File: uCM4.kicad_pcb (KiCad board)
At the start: 2 copper layers, 55 x 40 mm, 30 parts, among them J1 Conn_01x03, J2 Ethernet, J3 Micro_SD_Card, J4 USB_B_Micro, SW1 SW_DIP_x01, SW2 SW_DIP_x01, U1 RT9742GGJ5, U2 74LVC1G07, U3 TPD4EUSB30

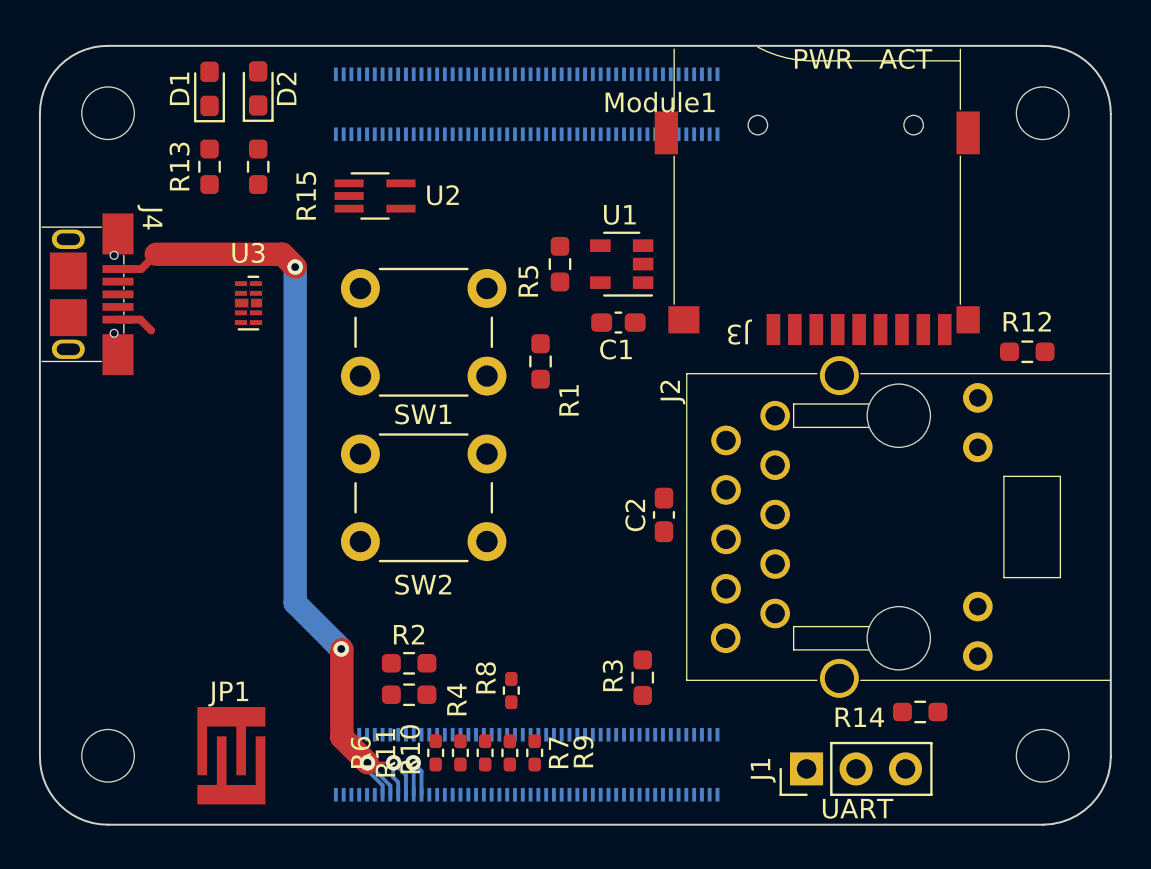
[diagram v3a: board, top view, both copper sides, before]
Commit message: Draw stands on Micro SD connector
It conflicts with mounting hole and this is the only problem on the
whole board at the moment. There are two ways to solve this, as it is
the only place where it (almost) fits:
1. Make ground plane of Micro SD a bit smaller - in the worst case will
   not mount connector to PCB
2. Remove mounting hole of module - will make two boards a little bit
   less stable together

As of now it is undecided what option to take.
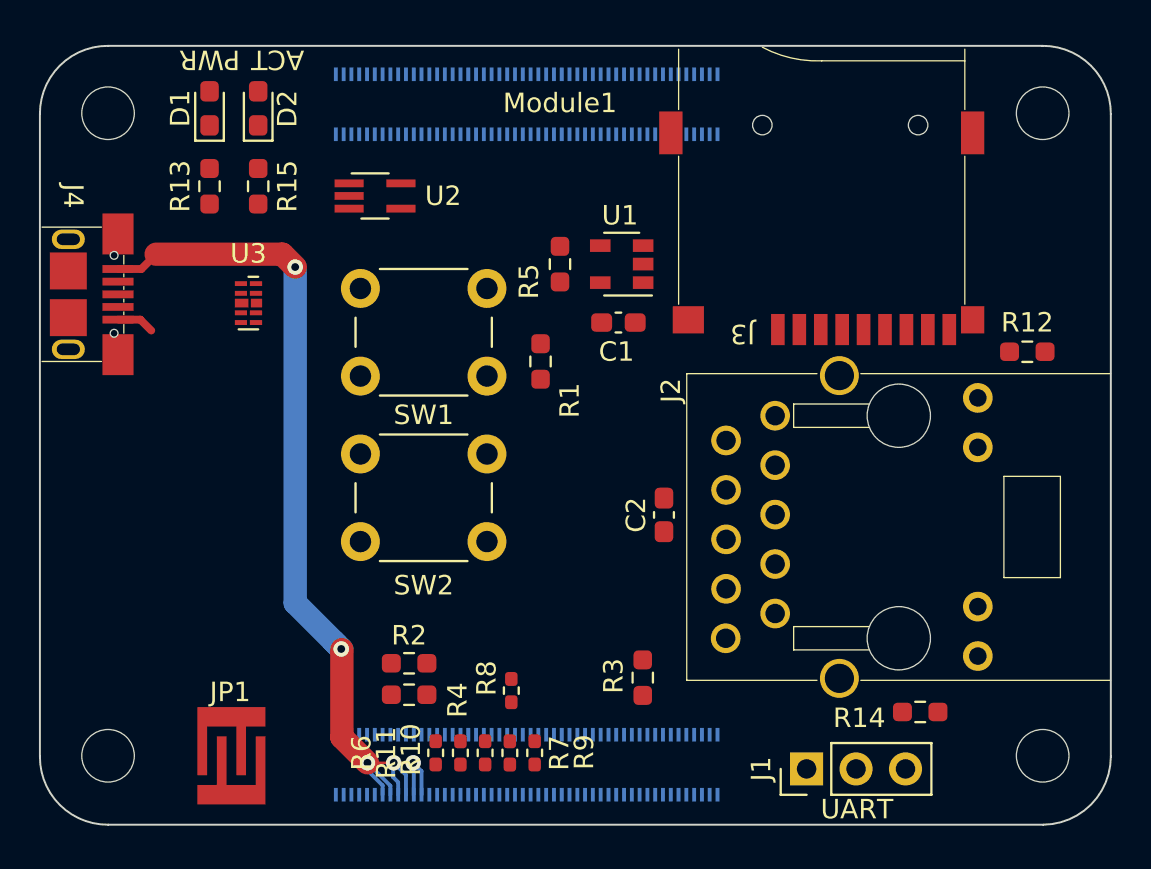
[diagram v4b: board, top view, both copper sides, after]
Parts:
- moved D2 1.02 mm to (149.0, 64.5)
- moved D1 1.00 mm to (146.5, 64.5)
- moved R13 1.00 mm to (146.5, 68.5)
- moved R15 1.00 mm to (149.0, 68.5)
- moved J3 0.23 mm to (177.9, 75.9)

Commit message: Route Micro SD connector
Hope this will not be moved anymore.
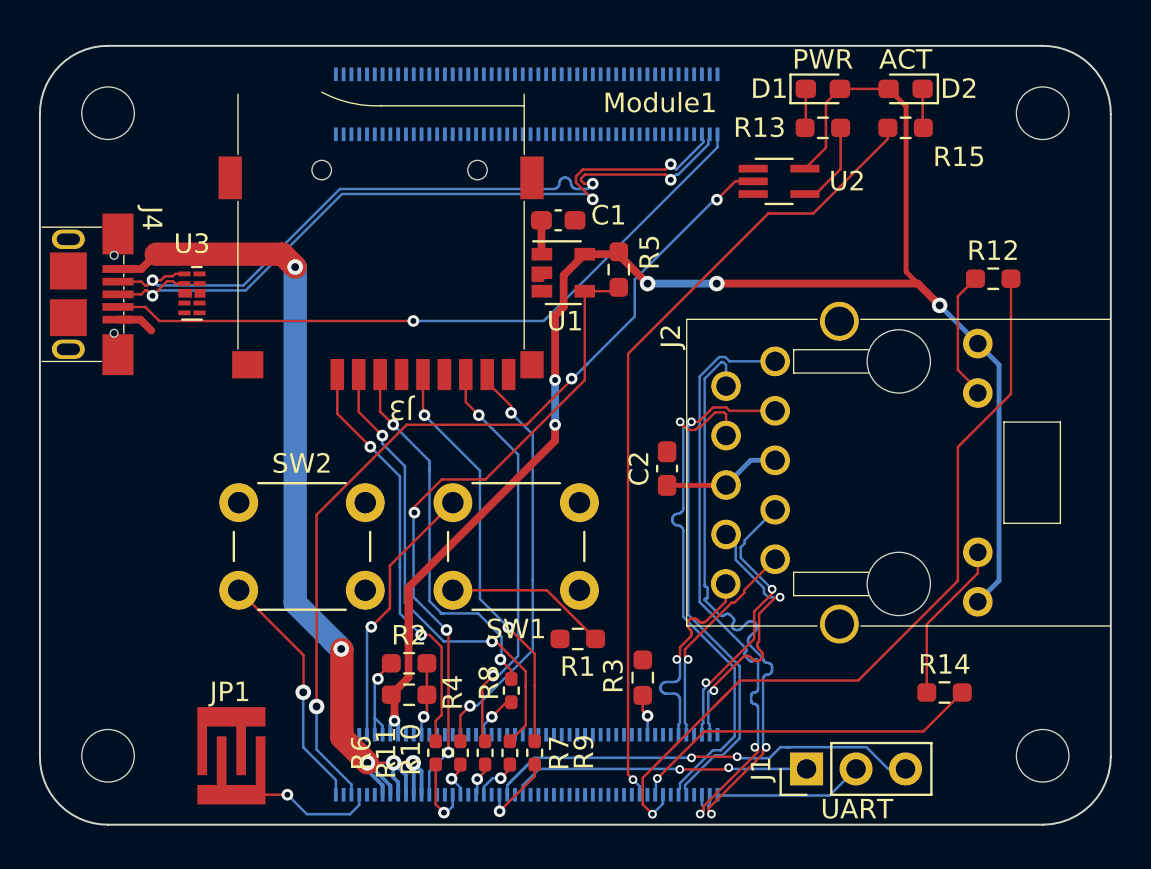
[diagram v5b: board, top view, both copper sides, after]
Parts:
- moved R15 33.4 mm to (182.2, 65.5), turned to 0 degrees
- moved D2 33.3 mm to (182.2, 63.5), turned to 180 degrees
- moved R13 31.6 mm to (178.0, 65.5), turned to 180 degrees
- moved D1 31.5 mm to (178.0, 63.5), turned to 0 degrees
- moved J3 22.7 mm to (155.3, 78.2)
- moved U2 20.8 mm to (175.8, 68.2)
- moved R1 14.4 mm to (165.4, 91.8), turned to 180 degrees
- moved SW1 12.0 mm to (165.5, 89.2)
- moved SW2 6.73 mm to (148.0, 84.8)
- moved C1 6.09 mm to (164.4, 70.2), turned to 180 degrees
- moved R12 4.14 mm to (186.8, 73.2), turned to 0 degrees
- moved R5 3.03 mm to (167.5, 72.8), turned to 90 degrees
- moved U1 3.03 mm to (164.7, 72.9), turned to 0 degrees
- moved U3 2.94 mm to (145.6, 74.0)
- moved J2 2.79 mm to (181.9, 83.2)
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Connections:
- net Net-(Module1-Pad57) renamed /SD_CLK
- net Net-(Module1-Pad61) renamed /SD_D3
- net Net-(Module1-Pad62) renamed /SD_CMD
- net Net-(Module1-Pad63) renamed /SD_D0
- net Net-(Module1-Pad67) renamed /SD_D1
- net Net-(Module1-Pad69) renamed /SD_D2
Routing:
- net +3V3: track 0.00 -> 87.6 mm, vias 0 -> 6
- net /nPWR_LED: track 0.00 -> 46.1 mm, vias 0 -> 3
- net Net-(Module1-Pad21): track 0.00 -> 41.5 mm, vias 0 -> 1
- net Net-(Module1-Pad15): track 0.00 -> 40.9 mm, vias 0 -> 1
- net /USB_P: track 0.00 -> 38.3 mm, vias 0 -> 3
- net /USB_N: track 0.00 -> 38.1 mm, vias 0 -> 3
- net Net-(J4-Pad4): track 0.00 -> 35.6 mm, vias 0 -> 1
- net /SD_EN: track 0.00 -> 34.0 mm, vias 0 -> 3
- net /Eth_P3_N: track 0.00 -> 31.3 mm, vias 0 -> 2
- net /Eth_P3_P: track 0.00 -> 31.3 mm, vias 0 -> 2
- net /Eth_P2_P: track 0.00 -> 26.4 mm, vias 0 -> 1
- net /Eth_P2_N: track 0.00 -> 26.4 mm, vias 0 -> 1
- net Net-(J3-Pad2): track 0.00 -> 24.4 mm, vias 0 -> 2
- net /TX: track 0.00 -> 24.1 mm, vias 0 -> 2
- net Net-(J3-Pad8): track 0.00 -> 21.6 mm, vias 0 -> 2
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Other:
- board text added: "1"
- board text added: "2"
- board text added: "3"
- board text added: "5"
- board text added: "7"
- board text added: "8"

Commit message: Reroute Ethernet and suroundings
All traces intersecting with Ethernet had to be removed to make
rerouting easier. Then Ethernet pairs were routed again. No length
adjustments has been done yet.
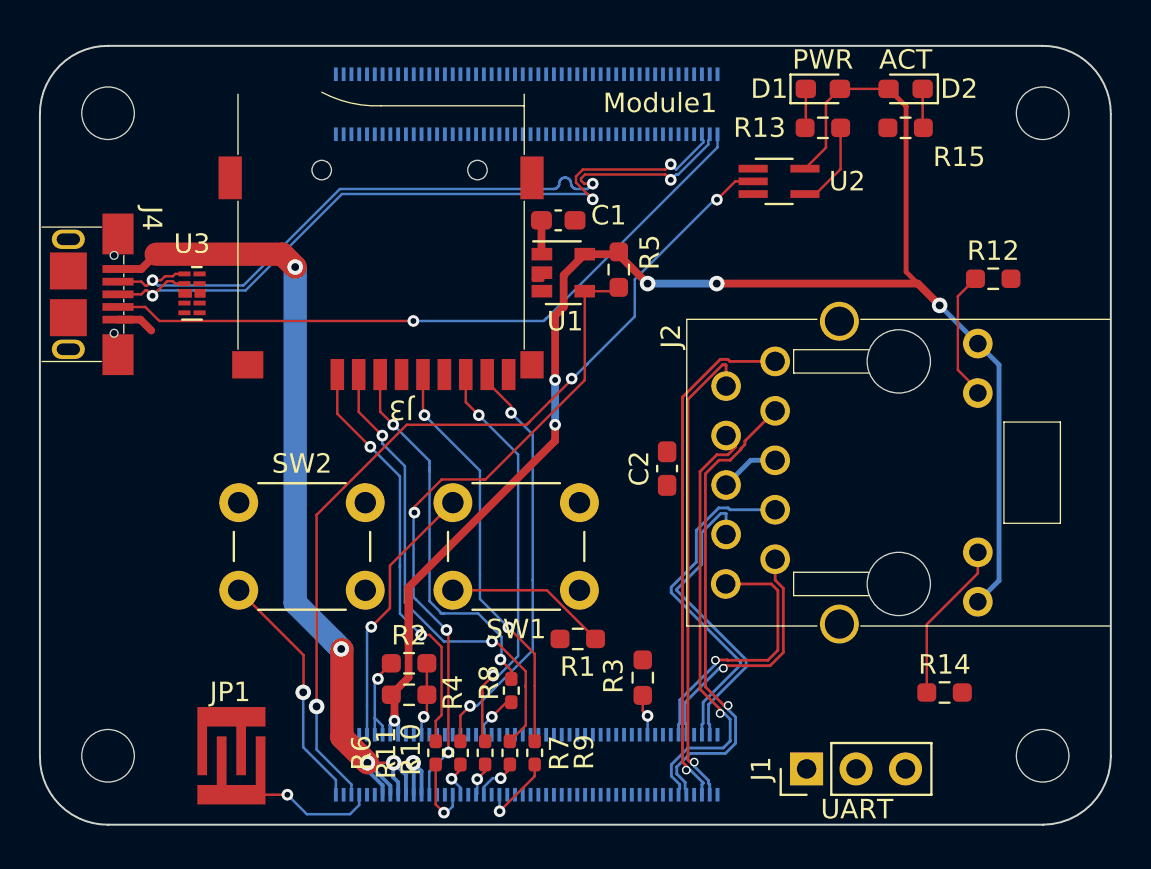
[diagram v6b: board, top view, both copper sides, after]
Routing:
- net Net-(Module1-Pad21): track 41.5 -> 0.00 mm, vias 1 -> 0
- net Net-(Module1-Pad15): track 40.9 -> 0.00 mm, vias 1 -> 0
- net /TX: track 24.1 -> 0.00 mm, vias 2 -> 0
- net Net-(Module1-Pad17): track 18.3 -> 0.00 mm, vias 1 -> 0
- net /RX: track 15.6 -> 0.00 mm, vias 2 -> 0
- net GND: track 10.1 -> 2.38 mm
- net /Eth_P3_P: track 31.3 -> 24.9 mm, vias 2 -> 1
- net /Eth_P3_N: track 31.3 -> 26.9 mm, vias 2 -> 1
- net /Eth_P2_P: track 26.4 -> 23.0 mm
- net /Eth_P1_N: track 14.6 -> 17.9 mm, vias 2 -> 0
- net Net-(C2-Pad1): track 6.08 -> 3.07 mm
- net /Eth_P0_P: track 11.2 -> 13.9 mm
- net /Eth_P2_N: track 26.4 -> 24.8 mm
- net /Eth_P0_N: track 11.2 -> 12.8 mm
- net /Eth_P1_P: track 14.6 -> 16.0 mm, vias 2 -> 0

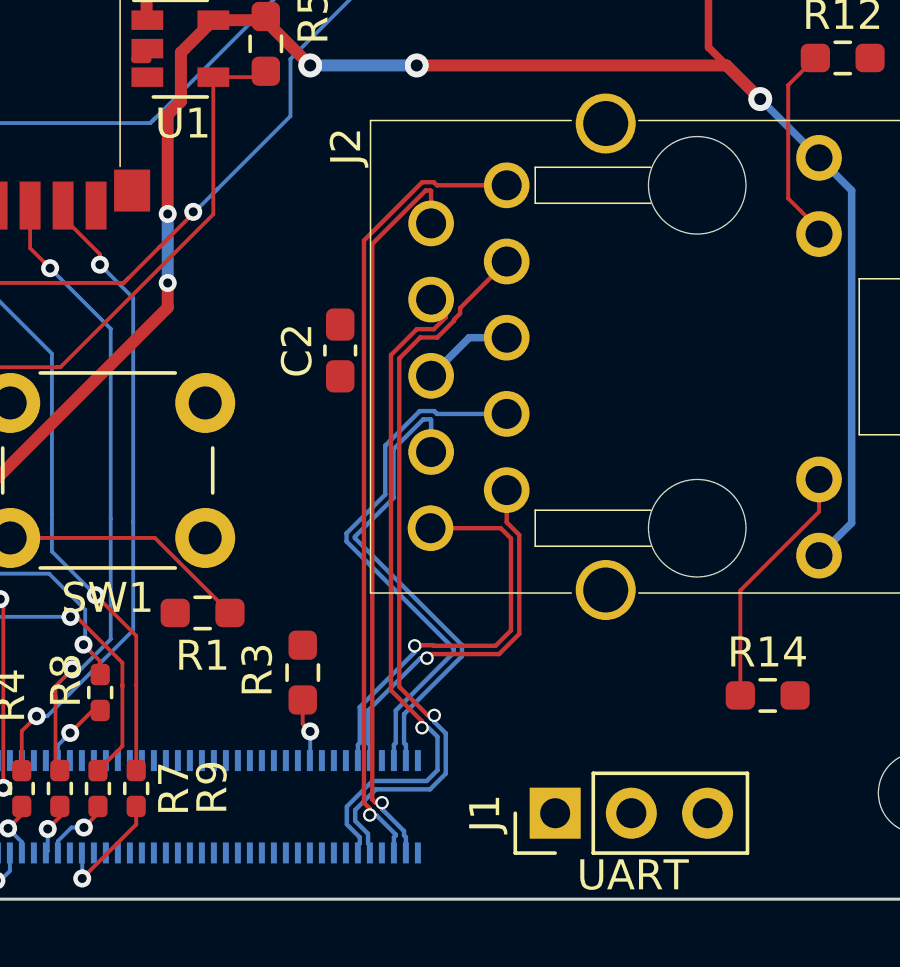
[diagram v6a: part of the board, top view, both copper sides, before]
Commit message: Adjust Ethernet pair and in-pair lengths
Almost complete - shortest path has in-pair difference of 0.8 mm. Let's
try again.
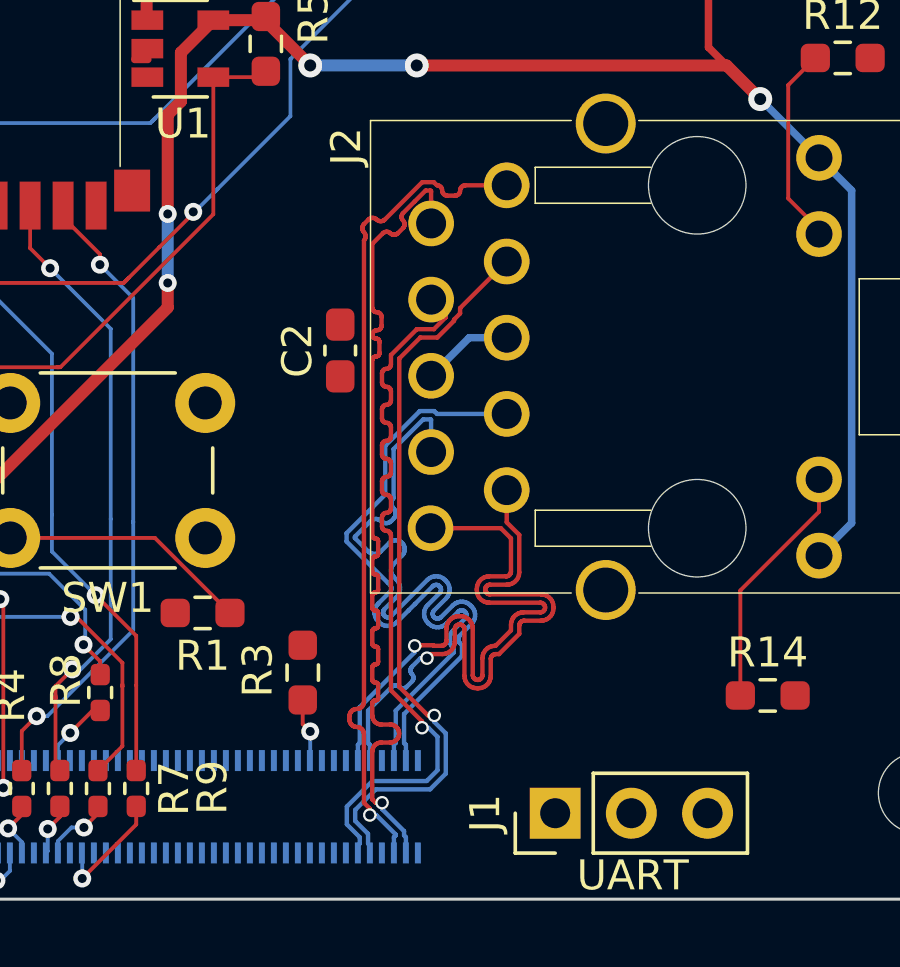
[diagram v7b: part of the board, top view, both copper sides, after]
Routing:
- net /Eth_P0_N: track 12.8 -> 20.5 mm
- net /Eth_P1_P: track 16.0 -> 23.6 mm
- net /Eth_P0_P: track 13.9 -> 21.3 mm
- net /Eth_P1_N: track 17.9 -> 23.5 mm
- net /Eth_P3_P: track 24.9 -> 28.3 mm
- net /Eth_P2_P: track 23.0 -> 24.7 mm
- net /Eth_P3_N: track 26.9 -> 28.2 mm

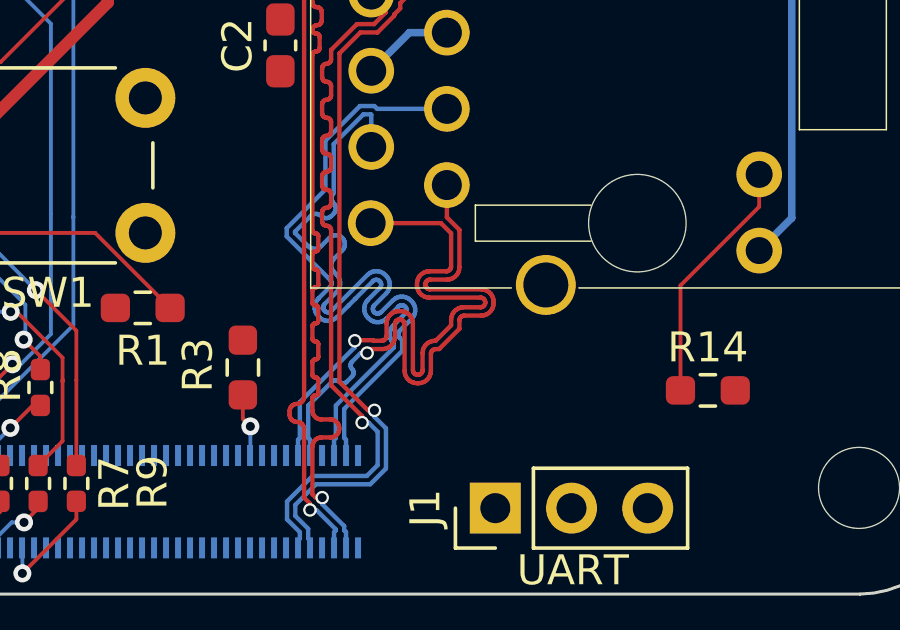
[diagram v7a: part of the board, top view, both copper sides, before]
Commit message: Fix zeroth Ethernet pair
Now it is in tolerance. Now it is a question, if another attempt for
pair-to-pair difference reduction makes any sense.
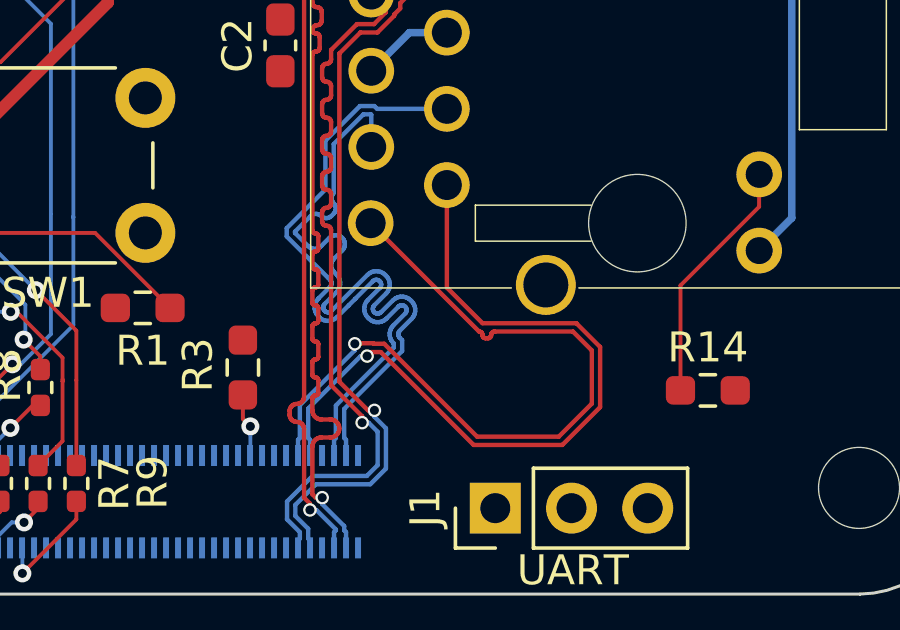
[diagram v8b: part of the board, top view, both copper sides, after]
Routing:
- net /Eth_P0_N: track 20.5 -> 25.3 mm
- net /Eth_P0_P: track 21.3 -> 25.3 mm
